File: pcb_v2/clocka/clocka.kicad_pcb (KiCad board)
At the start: 2 copper layers, 120 x 125 mm, 98 parts, among them J1 clock_ext, J26 bus clock, SW1 MANUAL, SW2 1HZ, SW3 1KHZ, SW4 XTAL1, SW5 XTAL2, SW6 EXT, SW7 CLOCK_SELECT, SW8 HALF-STEP, SW9 STEP, U1 74LS74, U10 74LS125, U11 NE555P, U12 NE555P, U2 74LS74, U3 74LS74, U4 74LS04, U5 74LS125, U6 74LS86, U7 74LS08, U8 NE555P, U9 NE555P, Y1 400KHz, Y2 1MHz

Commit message: Separado o painel de controle do gerador de clock
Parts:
- removed the C1 at (102.7, 58.5)
- removed the C10 at (102.7, 90.9)
- removed the C11 at (110.8, 58.5)
- removed the C2 at (102.7, 62.5)
- removed the C3 at (102.7, 66.6)
- removed the C4 at (102.7, 70.7)
- removed the C5 at (102.7, 74.7)
- removed the C6 at (102.7, 78.8)
- removed the C7 at (92.3, 100.2)
- removed the C8 at (102.7, 82.8)
- removed the C9 at (102.7, 86.8)
- added C15: 100nF, Capacitor_THT:C_Disc_D4.7mm_W2.5mm_P5.00mm, F.Cu at (268.6, 97.1)
- added C16: 100nF, Capacitor_THT:C_Disc_D4.7mm_W2.5mm_P5.00mm, F.Cu at (268.6, 83.1)
- added C17: 100nF, Capacitor_THT:C_Disc_D4.7mm_W2.5mm_P5.00mm, F.Cu at (268.6, 69.1)
- added C18: 100nF, Capacitor_THT:C_Disc_D4.7mm_W2.5mm_P5.00mm, F.Cu at (268.6, 40.6)
- added C19: 100nF, Capacitor_THT:C_Disc_D4.7mm_W2.5mm_P5.00mm, F.Cu at (252.7, 83.2)
- added C20: 100nF, Capacitor_THT:C_Disc_D4.7mm_W2.5mm_P5.00mm, F.Cu at (268.6, 55.2)
- added C21: 10nF, Capacitor_THT:C_Disc_D4.7mm_W2.5mm_P5.00mm, F.Cu at (138.5, 78.0)
- added C22: 10nF, Capacitor_THT:C_Disc_D4.7mm_W2.5mm_P5.00mm, F.Cu at (138.5, 82.1)
- added C23: 10nF, Capacitor_THT:C_Disc_D4.7mm_W2.5mm_P5.00mm, F.Cu at (138.5, 86.1)
- added C24: 10nF, Capacitor_THT:C_Disc_D4.7mm_W2.5mm_P5.00mm, F.Cu at (138.5, 90.2)
- added C25: 10uF, Capacitor_THT:CP_Radial_D5.0mm_P2.50mm, F.Cu at (147.2, 55.0)
- RV1, RV3: footprint Resistor_THT:R_Axial_DIN0207_L6.3mm_D2.5mm_P7.62mm_Horizontal -> Potentiometer_THT:Potentiometer_ACP_CA9-H5_Horizontal
- SW1: value MANUAL -> BREAK; footprint Button_Switch_THT:SW_PUSH_6mm -> Connector_JST:JST_XH_B2B-XH-AM_1x02_P2.50mm_Vertical
- SW2, SW3, SW4, SW5, SW6, SW8, SW9: footprint Button_Switch_THT:SW_PUSH_6mm -> Connector_JST:JST_XH_B2B-XH-AM_1x02_P2.50mm_Vertical
- SW7: footprint Connector_Molex:Molex_KK-254_AE-6410-02A_1x02_P2.54mm_Vertical -> Connector_JST:JST_XH_B2B-XH-AM_1x02_P2.50mm_Vertical
- moved SW5 230.9 mm to (274.3, 39.3), turned to 90 degrees
- moved SW1 227.7 mm to (274.3, 95.8), turned to 90 degrees
- moved SW4 226.6 mm to (274.3, 53.9), turned to 90 degrees
- moved SW2 225.1 mm to (274.3, 81.8), turned to 90 degrees
- moved SW3 224.7 mm to (274.3, 67.9), turned to 90 degrees
- moved R1 203.5 mm to (269.2, 101.6)
- moved R5 201.7 mm to (269.9, 45.1)
- moved SW9 201.5 mm to (258.4, 39.4), turned to 90 degrees
- moved R2 201.1 mm to (269.9, 87.6)
- moved R4 199.8 mm to (269.9, 59.7)
- moved R3 199.6 mm to (269.9, 73.7)
- moved SW6 199.6 mm to (258.4, 81.9), turned to 90 degrees
- moved SW8 198.6 mm to (258.4, 53.9), turned to 90 degrees
- moved R6 183.8 mm to (254.0, 87.6)
- moved C6 162.2 mm to (272.5, 114.9)
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- renumbered C21 to C1, C25 to C10, C15 to C11, C20 to C2, C19 to C3, C24 to C4, C22 to C5, C23 to C6, C26 to C7, C17 to C8, C28 to C9
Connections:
- D1 pad 1: set_clock_source -> Net-(D1-K)
- D2 pad 1: set_clock_source -> Net-(D1-K)
- D3 pad 1: set_clock_source -> Net-(D1-K)
- D4 pad 1: set_clock_source -> Net-(D1-K)
- D5 pad 1: set_clock_source -> Net-(D1-K)
- R7 pad 1: set_clock_source -> Net-(D1-K)
- U7 pad 10: +5V -> Net-(U7-Pad10)
- U7 pad 4: +5V -> Net-(D1-K)
- U7 pad 5: +5V -> Net-(D1-K)
- U7 pad 6: unconnected-(U7-Pad6) -> Net-(U7-Pad10)
- U7 pad 8: unconnected-(U7-Pad8) -> set_clock_source
- U7 pad 9: +5V -> Net-(U7-Pad10)

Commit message: layout de pcb do clock
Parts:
- removed C16, C17, C18, C19, C20: 100nF, Capacitor_THT:C_Disc_D4.7mm_W2.5mm_P5.00mm
- removed C25: 10uF, Capacitor_THT:CP_Radial_D5.0mm_P2.50mm
- removed D10: 1Hz, LED_THT:LED_D5.0mm
- removed D11: EXT, LED_THT:LED_D5.0mm
- removed D12: XTAL2, LED_THT:LED_D5.0mm
- removed D19: CLOCK PULSE, LED_THT:LED_D5.0mm
- removed D8: 1KHz, LED_THT:LED_D5.0mm
- removed D9: XTAL1, LED_THT:LED_D5.0mm
- removed J1: clock_ext, Connector_Molex:Molex_KK-254_AE-6410-02A_1x02_P2.54mm_Vertical
- removed R1, R15, R17, R2, R21, R3, R4, R5, R6: 10K, Resistor_THT:R_Axial_DIN0207_L6.3mm_D2.5mm_P7.62mm_Horizontal
- removed R10, R11, R12, R25, R8, R9: 1K, Resistor_THT:R_Axial_DIN0207_L6.3mm_D2.5mm_P7.62mm_Horizontal
- removed SW1: BREAK, Connector_JST:JST_XH_B2B-XH-AM_1x02_P2.50mm_Vertical
- removed SW2: 1HZ, Connector_JST:JST_XH_B2B-XH-AM_1x02_P2.50mm_Vertical
- removed SW3: 1KHZ, Connector_JST:JST_XH_B2B-XH-AM_1x02_P2.50mm_Vertical
- removed SW4: XTAL1, Connector_JST:JST_XH_B2B-XH-AM_1x02_P2.50mm_Vertical
- removed SW5: XTAL2, Connector_JST:JST_XH_B2B-XH-AM_1x02_P2.50mm_Vertical
- removed SW6: EXT, Connector_JST:JST_XH_B2B-XH-AM_1x02_P2.50mm_Vertical
- removed SW7: CLOCK_SELECT, Connector_JST:JST_XH_B2B-XH-AM_1x02_P2.50mm_Vertical
- removed SW8: HALF-STEP, Connector_JST:JST_XH_B2B-XH-AM_1x02_P2.50mm_Vertical
- removed SW9: STEP, Connector_JST:JST_XH_B2B-XH-AM_1x02_P2.50mm_Vertical
- added J26: bus clock, Connector_PinHeader_2.54mm:PinHeader_2x08_P2.54mm_Vertical, F.Cu at (249.6, 128.9)
- added J3: control panel, Connector_PinHeader_2.54mm:PinHeader_2x08_P2.54mm_Vertical, F.Cu at (249.6, 138.4)
- C15: value 100nF -> 10uF
- J2: renamed from J26; value bus clock -> control panel
- moved D1 220.6 mm to (238.1, 140.3), turned to 180 degrees
- moved D3 218.9 mm to (238.1, 143.5), turned to 180 degrees
- moved D4 218.8 mm to (238.1, 146.7), turned to 180 degrees
- moved D2 217.8 mm to (238.1, 137.2), turned to 180 degrees
- moved D5 212.7 mm to (238.1, 134.0), turned to 180 degrees
- moved D18 197.7 mm to (234.9, 108.0), turned to 180 degrees
- moved D6 196.8 mm to (217.2, 146.7)
- moved D13 194.0 mm to (217.2, 143.5)
- moved D14 191.5 mm to (217.2, 140.3)
- moved D15 189.2 mm to (217.2, 137.2)
- moved D16 187.1 mm to (217.2, 134.0)
- moved R7 174.5 mm to (238.1, 130.8), turned to 180 degrees
- moved D17 164.1 mm to (202.6, 81.3)
- moved D20 161.1 mm to (199.4, 81.3), turned to 180 degrees
- moved R22 153.9 mm to (234.9, 100.3), turned to 180 degrees
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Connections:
- net Net-(D17-K) renamed clock_pulse
- C15 pad 1: ~{operator_break_enable} -> GND
- C15 pad 2: ~{operator_break} -> Net-(U8-THR)
- J2 pad 10: RESET -> ~{operator_break}
- J2 pad 11: unconnected-(J26-Pin_11-Pad11) -> set_clock_xtal1
- J2 pad 12: unconnected-(J26-Pin_12-Pad12) -> set_clock_xtal2
- J2 pad 13: unconnected-(J26-Pin_13-Pad13) -> set_clock_1hz
- J2 pad 14: ~{CLOCK} -> set_clock_1Khz
- J2 pad 3: unconnected-(J26-Pin_3-Pad3) -> Net-(J2-Pin_3)
- J2 pad 4: CLOCK -> Net-(J2-Pin_4)
- J2 pad 5: unconnected-(J26-Pin_5-Pad5) -> Net-(J2-Pin_5)
- J2 pad 6: ~{control_break} -> Net-(J2-Pin_6)
- J2 pad 7: unconnected-(J26-Pin_7-Pad7) -> ~{operator_break_enable}
- J2 pad 8: unconnected-(J26-Pin_8-Pad8) -> Net-(J2-Pin_8)
- J2 pad 9: unconnected-(J26-Pin_9-Pad9) -> set_clock_ext
- RV1 pad 1: Net-(R14-Pad1) -> unconnected-(RV1-Pad1)
- RV1 pad 3: unconnected-(RV1-Pad3) -> Net-(R14-Pad1)
- RV3 pad 1: Net-(R27-Pad1) -> unconnected-(RV3-Pad1)
- RV3 pad 3: unconnected-(RV3-Pad3) -> Net-(R27-Pad1)
- U11 pad 2: Net-(U11-TR) -> step
- U12 pad 2: Net-(U12-TR) -> half_step
- U4 pad 10: Net-(C20-Pad1) -> Net-(J2-Pin_6)
- U4 pad 2: Net-(C16-Pad1) -> Net-(J2-Pin_4)
- U4 pad 4: Net-(C17-Pad1) -> Net-(J2-Pin_3)
- U4 pad 6: Net-(C18-Pad1) -> Net-(J2-Pin_5)
- U4 pad 8: Net-(C19-Pad1) -> Net-(J2-Pin_8)
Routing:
- net +5V: track 0.00 -> 633.2 mm
- net ~{control_break}: track 0.00 -> 163.9 mm, vias 0 -> 4
- net clock_1hz: track 0.00 -> 156.8 mm, vias 0 -> 3
- net clock_xtal2: track 0.00 -> 153.3 mm, vias 0 -> 3
- net clock_pulse: track 0.00 -> 144.1 mm, vias 0 -> 2
- net clock_ext: track 0.00 -> 142.2 mm, vias 0 -> 3
- net signal_xtal1: track 0.00 -> 141.4 mm, vias 0 -> 2
- net signal_1KHz: track 0.00 -> 129.7 mm, vias 0 -> 5
- net RESET: track 0.00 -> 129.6 mm, vias 0 -> 2
- net Net-(D1-K): track 0.00 -> 123.1 mm, vias 0 -> 2
- net ~{disengage_clock}: track 0.00 -> 111.7 mm, vias 0 -> 3
- net signal_1Hz: track 0.00 -> 110.4 mm, vias 0 -> 2
- net set_clock_1hz: track 0.00 -> 105.5 mm, vias 0 -> 2
- net signal_xtal2: track 0.00 -> 104.7 mm
- net set_clock_source: track 0.00 -> 102.5 mm, vias 0 -> 2
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- added copper zone on B.Cu, net GND
- added copper zone on F.Cu, net GND
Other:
- outline, holes or cut-outs redrawn

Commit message: layout concluído
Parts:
- moved U2 33.6 mm to (263.5, 99.1)
- moved C2 33.6 mm to (266.1, 95.2)
- moved D5 25.9 mm to (214.0, 143.5), turned to 0 degrees
- moved D3 24.3 mm to (214.0, 146.7), turned to 0 degrees
- moved D1 14.8 mm to (224.8, 146.7), turned to 0 degrees
- moved D2 14.8 mm to (224.8, 143.5), turned to 0 degrees
- moved D4 14.8 mm to (224.8, 140.3), turned to 0 degrees
- moved D13 9.92 mm to (224.8, 137.2)
- moved D18 9.53 mm to (234.9, 98.4)
- moved D15 8.25 mm to (224.8, 134.0)
- moved D6 7.10 mm to (214.0, 140.3)
- moved C11 5.72 mm to (219.1, 98.4)
- moved C13 5.72 mm to (232.3, 102.2)
- moved C14 5.72 mm to (232.3, 75.6)
- moved C15 5.72 mm to (196.8, 79.4)
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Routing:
- net Net-(J2-Pin_6): track 9.31 -> 132.2 mm, vias 0 -> 3
- net ~{operator_break}: track 75.1 -> 196.9 mm, vias 2 -> 3
- net Net-(J2-Pin_8): track 1.80 -> 118.6 mm, vias 0 -> 1
- net ~{operator_break_enable}: track 0.00 -> 113.4 mm, vias 0 -> 2
- net set_clock_xtal2: track 67.6 -> 178.6 mm, vias 2 -> 3
- net set_clock_xtal1: track 2.69 -> 113.4 mm, vias 0 -> 2
- net set_clock_1hz: track 105.5 -> 199.2 mm, vias 2 -> 3
- net set_clock_1Khz: track 2.80 -> 91.4 mm, vias 0 -> 2
- net signal_ext: track 56.2 -> 142.6 mm, vias 2 -> 3
- net set_clock_ext: track 87.2 -> 166.6 mm, vias 2 -> 3
- net ~{clock_manual}: track 90.4 -> 162.4 mm, vias 0 -> 1
- net step: track 10.2 -> 80.6 mm, vias 0 -> 1
- net Net-(J2-Pin_5): track 70.6 -> 139.3 mm, vias 0 -> 3
- net Net-(D1-K): track 123.1 -> 185.6 mm
- net Net-(J2-Pin_4): track 84.9 -> 146.6 mm, vias 0 -> 3
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
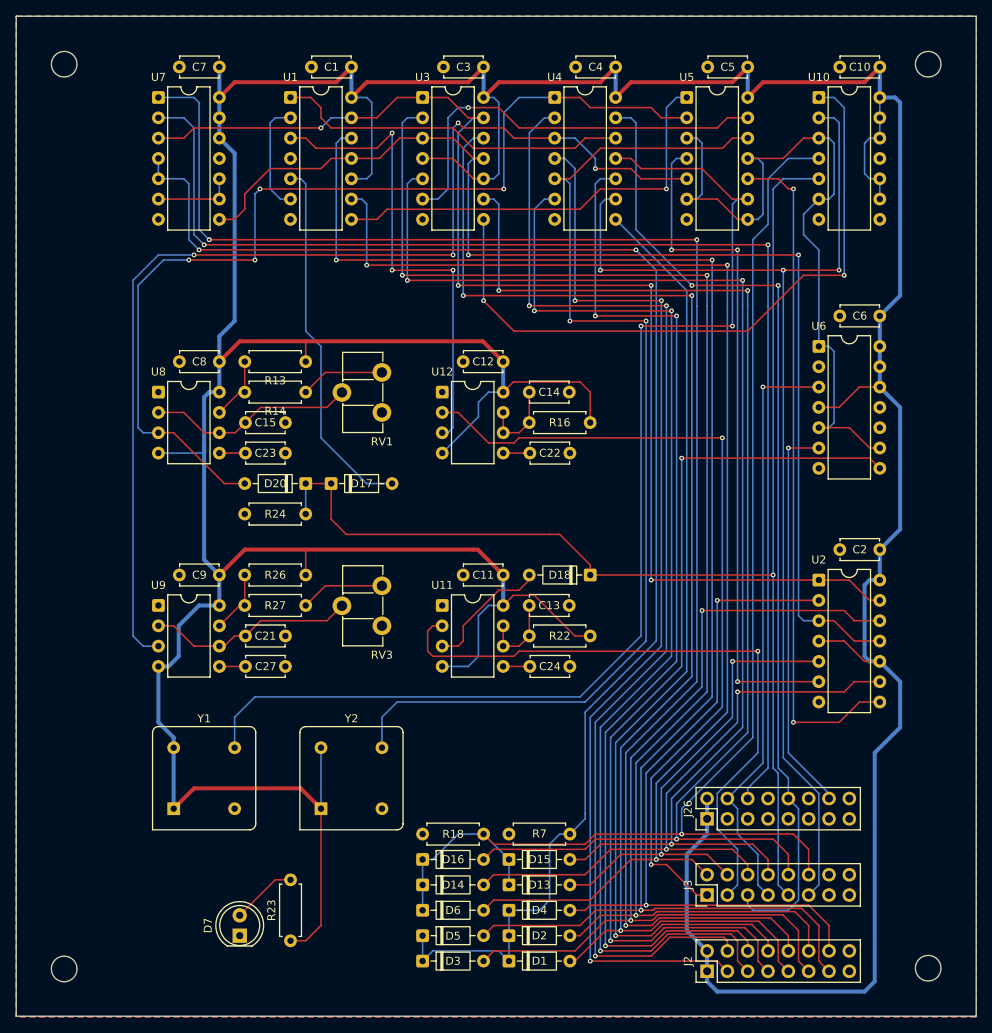
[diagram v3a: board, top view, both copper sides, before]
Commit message: pcb reduzida; iniciando um novo layout com inversão na posição dos chips
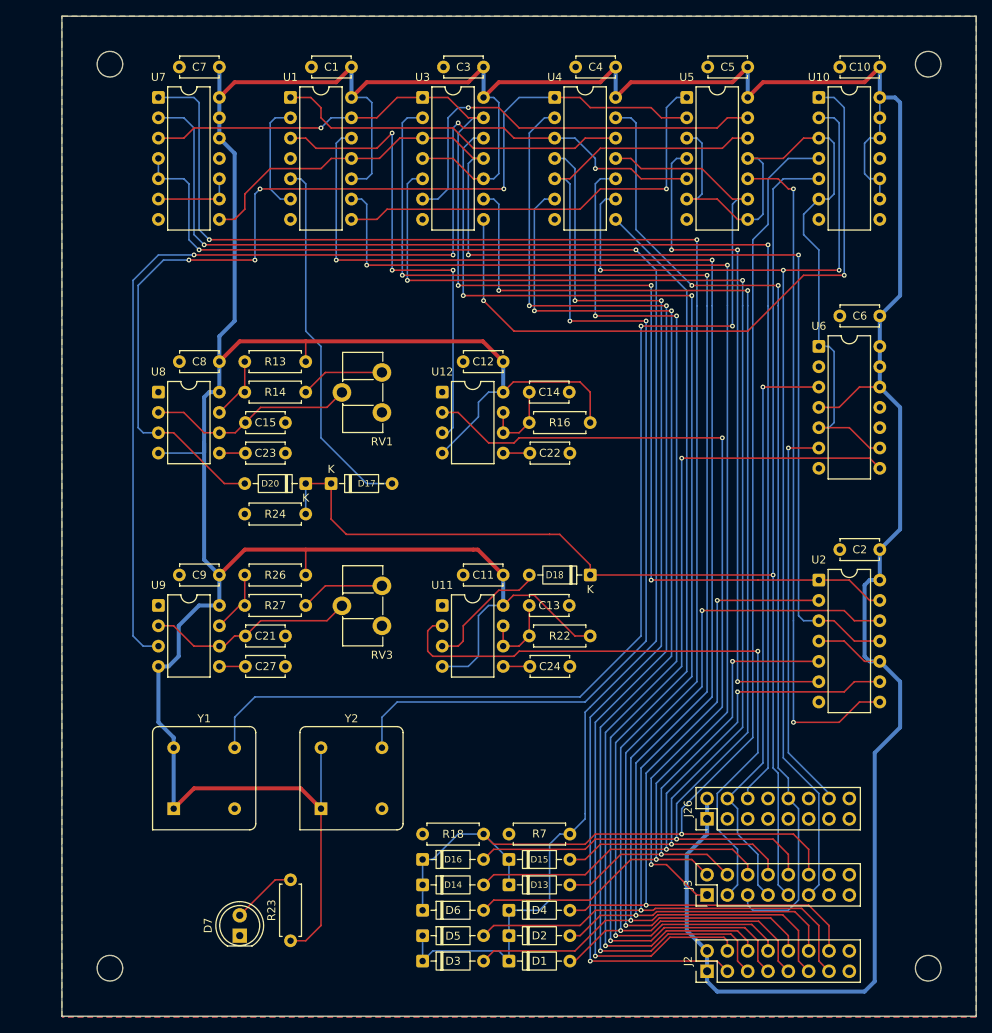
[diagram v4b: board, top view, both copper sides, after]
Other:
- board size 120 x 125 mm -> 114.3 x 125 mm
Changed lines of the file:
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@@
 		(tags "Resistor Axial_DIN0207 series Axial Horizontal pin pitch 7.62mm 0.25W = 1/4W length 6.3mm diameter 2.5mm")
 		(property "Reference" "R14"
-			(at 3.81 -2.37 0)
+			(at 3.81 0 0)
 			(layer "F.SilkS")
 			(effects
@@
 			(effects
 				(font
-					(size 1 1)
-					(thickness 0.15)
+					(size 0.8 0.8)
+					(thickness 0.1)
 				)
 			)
@@
 			(effects
 				(font
-					(size 1 1)
-					(thickness 0.15)
+					(size 0.8 0.8)
+					(thickness 0.1)
 				)
 			)
@@
 			(layer "F.SilkS")
 		)
-		(fp_line
-			(start 4.32 -1.77)
-			(end -1.77 -1.77)
-			(stroke
-				(width 0.05)
-				(type solid)
-			)
-			(layer "F.CrtYd")
-		)
-		(fp_line
+		(fp_rect
 			(start -1.77 -1.77)
-			(end -1.77 19.55)
-			(stroke
-				(width 0.05)
-				(type solid)
-			)
-			(layer "F.CrtYd")
-		)
-		(fp_line
-			(start 4.32 19.55)
-			(end 4.32 -1.77)
-			(stroke
-				(width 0.05)
-				(type solid)
-			)
-			(layer "F.CrtYd")
-		)
-		(fp_line
-			(start -1.77 19.55)
 			(end 4.32 19.55)
 			(stroke
@@
 				(type solid)
 			)
+			(fill no)
 			(layer "F.CrtYd")
 		)
@@
 			(effects
 				(font
-					(size 1 1)
-					(thickness 0.15)
+					(size 0.8 0.8)
+					(thickness 0.1)
 				)
 			)
@@
 		(tags "Resistor Axial_DIN0207 series Axial Horizontal pin pitch 7.62mm 0.25W = 1/4W length 6.3mm diameter 2.5mm")
 		(property "Reference" "R13"
-			(at 3.81 -2.37 0)
+			(at 3.81 0 0)
 			(layer "F.SilkS")
 			(effects
@@
 		(tags "Diode DO-35_SOD27 series Axial Horizontal pin pitch 7.62mm  length 4mm diameter 2mm")
 		(property "Reference" "D17"
-			(at 3.81 0 0)
+			(at 4.45 0 0)
 			(layer "F.SilkS")
 			(effects
 				(font
-					(size 1 1)
-					(thickness 0.15)
+					(size 0.8 0.8)
+					(thickness 0.1)
 				)
 			)
@@
 		(fp_text user "K"
 			(at 0 -1.8 0)
+			(layer "F.SilkS")
+			(effects
+				(font
+					(size 1 1)
+					(thickness 0.15)
+				)
+			)
+		)
+		(fp_text user "K"
+			(at 0 -1.8 0)
 			(layer "F.Fab")
 			(effects
@@
 			(layer "F.SilkS")
 		)
-		(fp_line
-			(start 4.49 -3.21)
-			(end -1.94 -3.21)
-			(stroke
-				(width 0.05)
-				(type solid)
-			)
-			(layer "F.CrtYd")
-		)
-		(fp_line
+		(fp_rect
 			(start -1.94 -3.21)
-			(end -1.94 3.21)
-			(stroke
-				(width 0.05)
-				(type solid)
-			)
-			(layer "F.CrtYd")
-		)
-		(fp_line
-			(start 4.49 3.21)
-			(end 4.49 -3.21)
-			(stroke
-				(width 0.05)
-				(type solid)
-			)
-			(layer "F.CrtYd")
-		)
-		(fp_line
-			(start -1.94 3.21)
 			(end 4.49 3.21)
 			(stroke
@@
 				(type solid)
 			)
+			(fill no)
 			(layer "F.CrtYd")
 		)
@@
 			(effects
 				(font
-					(size 1 1)
-					(thickness 0.15)
+					(size 0.8 0.8)
+					(thickness 0.1)
 				)
 			)
@@
 		(tags "Diode DO-35_SOD27 series Axial Horizontal pin pitch 7.62mm  length 4mm diameter 2mm")
 		(property "Reference" "D20"
-			(at 3.81 0 0)
+			(at 4.44 0 0)
 			(layer "F.SilkS")
 			(effects
 				(font
-					(size 1 1)
-					(thickness 0.15)
+					(size 0.8 0.8)
+					(thickness 0.1)
 				)
 			)
@@
 		)
 		(fp_text user "K"
+			(at 0 -1.8 180)
+			(layer "F.SilkS")
+			(effects
+				(font
+					(size 1 1)
+					(thickness 0.15)
+				)
+			)
+		)
+		(fp_text user "K"
 			(at 0 -1.8 0)
 			(layer "F.Fab")
@@
 		(tags "Diode DO-35_SOD27 series Axial Horizontal pin pitch 7.62mm  length 4mm diameter 2mm")
 		(property "Reference" "D18"
-			(at 3.81 0 0)
+			(at 4.445 0 0)
 			(layer "F.SilkS")
 			(effects
 				(font
-					(size 1 1)
-					(thickness 0.15)
+					(size 0.9 0.8)
+					(thickness 0.1)
 				)
 			)
@@
 		)
 		(fp_text user "K"
+			(at 0 -1.8 180)
+			(layer "F.SilkS")
+			(effects
+				(font
+					(size 1 1)
+					(thickness 0.15)
+				)
+			)
+		)
+		(fp_text user "K"
 			(at 0 -1.8 0)
 			(layer "F.Fab")
@@
 	)
 	(gr_circle
-		(center 169.195 34.575)
-		(end 170.795 34.575)
+		(center 174.91 34.575)
+		(end 176.51 34.575)
 		(stroke
 			(width 0.05)
@@
 	)
 	(gr_circle
-		(center 169.195 147.67)
-		(end 170.795 147.67)
+		(center 174.91 147.575)
+		(end 176.51 147.575)
 		(stroke
 			(width 0.05)
@@
 	)
 	(gr_rect
-		(start 163.195 28.575)
+		(start 168.91 28.575)
 		(end 283.195 153.575)
 		(stroke
@@
 		(polygon
 			(pts
-				(xy 163.195 28.575) (xy 283.21 28.575) (xy 283.21 153.67) (xy 163.195 153.67)
+				(xy 168.91 28.575) (xy 283.21 28.575) (xy 283.21 153.67) (xy 168.91 153.67)
 			)
 		)

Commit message: novo layout do pcb
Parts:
- moved Y2 100.3 mm to (261.0, 47.0)
- moved Y1 100.3 mm to (242.6, 47.0)
- moved D7 77.8 mm to (268.0, 131.4)
- moved R23 77.8 mm to (274.3, 132.1)
- moved C7 58.5 mm to (180.4, 93.3)
- moved U7 58.5 mm to (177.8, 97.2)
- moved C1 58.5 mm to (198.2, 93.3)
- moved U1 58.5 mm to (195.6, 97.2)
- moved C4 58.4 mm to (233.8, 93.3)
- moved C5 58.4 mm to (250.3, 93.3)
- moved U4 58.4 mm to (231.1, 97.2)
- moved U5 58.4 mm to (247.7, 97.2)
- moved C3 58.4 mm to (216.0, 93.3)
- moved U3 58.4 mm to (213.4, 97.2)
- moved RV3 40.0 mm to (182.2, 74.9)
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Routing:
- net +5V: track 648.2 -> 435.5 mm
- net Net-(D1-K): track 185.6 -> 2.54 mm, vias 2 -> 0
- net ~{operator_break}: track 196.9 -> 21.1 mm, vias 3 -> 0
- net set_clock_1hz: track 199.2 -> 30.5 mm, vias 3 -> 0
- net clock_1hz: track 164.2 -> 0.00 mm, vias 3 -> 0
- net ~{clock_manual}: track 162.4 -> 0.00 mm, vias 1 -> 0
- net ~{control_break}: track 160.9 -> 0.00 mm, vias 2 -> 0
- net clock_ext: track 158.8 -> 0.00 mm, vias 3 -> 0
- net clock_xtal2: track 158.6 -> 0.00 mm, vias 3 -> 0
- net set_clock_xtal2: track 178.6 -> 24.8 mm, vias 3 -> 0
- net signal_xtal1: track 145.6 -> 0.00 mm, vias 2 -> 0
- net set_clock_ext: track 166.6 -> 22.2 mm, vias 3 -> 0
- net signal_ext: track 142.6 -> 0.00 mm, vias 3 -> 0
- net signal_1KHz: track 138.5 -> 0.00 mm, vias 4 -> 0
- net Net-(J2-Pin_4): track 146.6 -> 8.70 mm, vias 3 -> 0
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
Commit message: Novo layout concluído
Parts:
- Y1: value 400KHz -> XTAL1
- Y2: value 1MHz -> XTAL2
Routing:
- net +5V: track 435.5 -> 604.9 mm
- net ~{clock_manual}: track 0.00 -> 165.2 mm, vias 0 -> 2
- net CLOCK: track 0.00 -> 147.7 mm, vias 0 -> 2
- net clock_xtal1: track 0.00 -> 135.7 mm, vias 0 -> 2
- net ~{operator_break_enable}: track 17.9 -> 145.6 mm, vias 0 -> 2
- net set_clock_xtal1: track 26.0 -> 149.8 mm, vias 0 -> 2
- net ~{control_break}: track 0.00 -> 117.7 mm, vias 0 -> 2
- net clock_1Khz: track 0.00 -> 115.3 mm, vias 0 -> 3
- net combined_clock: track 0.00 -> 112.4 mm, vias 0 -> 1
- net half_step: track 0.00 -> 109.4 mm
- net signal_1KHz: track 0.00 -> 107.7 mm, vias 0 -> 3
- net set_clock_1Khz: track 29.1 -> 132.1 mm, vias 0 -> 3
- net signal_xtal2: track 0.00 -> 99.4 mm, vias 0 -> 1
- net signal_xtal1: track 0.00 -> 95.6 mm, vias 0 -> 1
- net clock_pulse: track 46.3 -> 139.8 mm, vias 0 -> 1
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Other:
- board text added: "1Hz"
- board text added: "1KHz"
- board text added: "A"
- board text added: "B"
- board text added: "CLOCK"
